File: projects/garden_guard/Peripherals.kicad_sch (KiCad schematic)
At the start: 13 parts, among them J10 Conn_02x06_Odd_Even, J11 Conn_02x01, J12 Conn_02x01, J9 Conn_02x05_Odd_Even, U11 DMN2028USS-13, U12 DMN2028USS-13

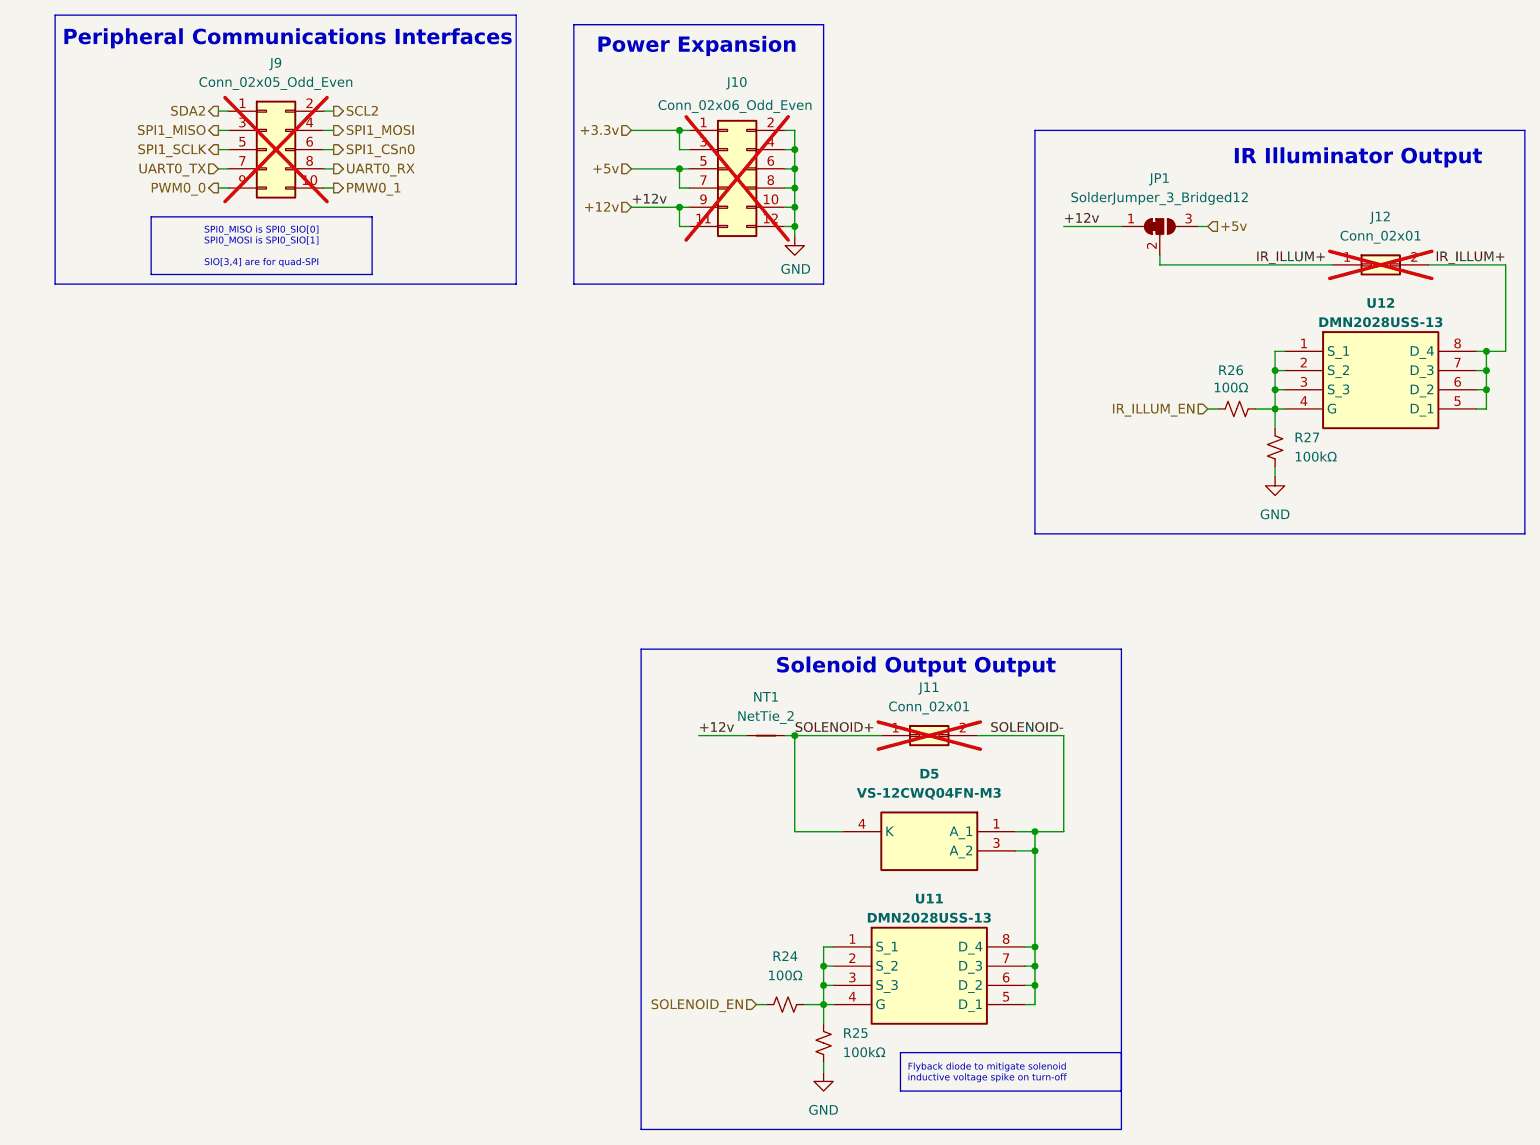
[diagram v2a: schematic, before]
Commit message: - Assign 3D models to lingering footprints lacking them - Start playing with board layout - Move CM5 library files from project to components dir
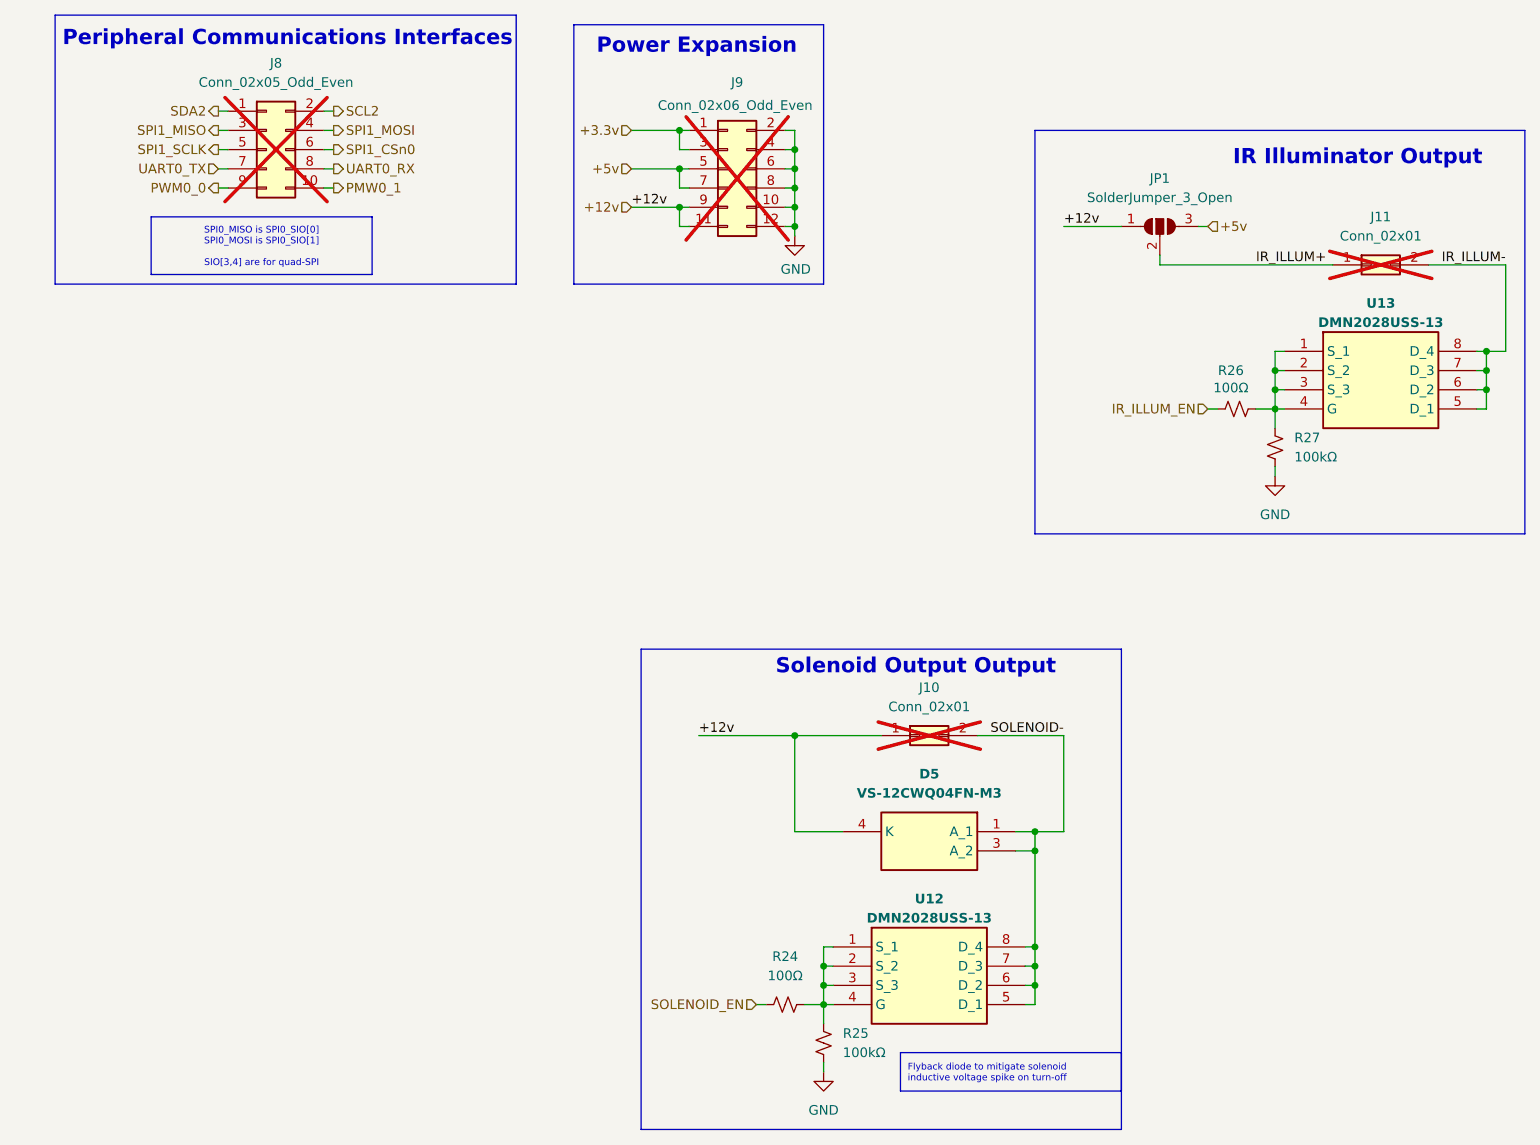
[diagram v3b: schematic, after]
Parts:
- removed JP1: SolderJumper_3_Bridged12, Jumper:SolderJumper-3_P1.3mm_Bridged12_RoundedPad1.0x1.5mm, symbol Jumper:SolderJumper_3_Bridged12
- removed NT1: NetTie_2, NetTie:NetTie-2_SMD_Pad0.5mm, symbol Device:NetTie_2
- added JP1: SolderJumper_3_Open, Jumper:SolderJumper-3_P1.3mm_Open_RoundedPad1.0x1.5mm, symbol Jumper:SolderJumper_3_Open
- renumbered J11 to J10, J12 to J11, J9 to J8, J10 to J9, U11 to U12, U12 to U13
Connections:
- net SOLENOID+ is gone; now on net +12v: D5.4 (K), J10.1 (Pin_1)
- net +12v: now also JP1.1 (A)
- net +5v: now also JP1.3 (B)
- net IR_ILLUM+: now also JP1.2 (C); no longer J11.2 (Pin_2), U13.5 (D_1), U13.6 (D_2), U13.7 (D_3), U13.8 (D_4)
- new net IR_ILLUM-: J11.2 (Pin_2), U13.5 (D_1), U13.6 (D_2), U13.7 (D_3), U13.8 (D_4)
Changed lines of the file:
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@@
 	(wire
 		(pts
-			(xy 114.3 123.19) (xy 120.65 123.19)
+			(xy 114.3 123.19) (xy 127 123.19)
 		)
 		(stroke
@@
 		(pts
 			(xy 217.17 77.47) (xy 218.44 77.47)
-		)
-		(stroke
-			(width 0)
-			(type default)
-		)
-	)
-	(wire
-		(pts
-			(xy 125.73 123.19) (xy 127 123.19)
 		)
 		(stroke
@@
 		)
 	)
-	(label "IR_ILLUM+"
+	(label "IR_ILLUM-"
 		(at 220.98 60.96 180)
 		(effects
@@
 			)
 			(justify right bottom)
-		)
-	)
-	(label "SOLENOID+"
-		(at 127 123.19 0)
-		(effects
-			(font
-				(size 1.27 1.27)
-			)
-			(justify left bottom)
 		)
 	)
@@
 	)
 	(symbol
-		(lib_id "Device:NetTie_2")
-		(at 123.19 123.19 0)
+		(lib_id "Jumper:SolderJumper_3_Open")
+		(at 175.26 55.88 0)
 		(unit 1)
 		(exclude_from_sim no)
@@
 		(dnp no)
 		(fields_autoplaced yes)
-		(property "Reference" "NT1"
-			(at 123.19 118.11 0)
-			(effects
-				(font
-					(size 1.27 1.27)
-				)
-			)
-		)
-		(property "Value" "NetTie_2"
-			(at 123.19 120.65 0)
-			(effects
-				(font
-					(size 1.27 1.27)
-				)
-			)
-		)
-		(property "Footprint" "NetTie:NetTie-2_SMD_Pad0.5mm"
-			(at 123.19 123.19 0)
+		(property "Reference" "JP1"
+			(at 175.26 49.53 0)
+			(effects
+				(font
+					(size 1.27 1.27)
+				)
+			)
+		)
+		(property "Value" "SolderJumper_3_Open"
+			(at 175.26 52.07 0)
+			(effects
+				(font
+					(size 1.27 1.27)
+				)
+			)
+		)
+		(property "Footprint" "Jumper:SolderJumper-3_P1.3mm_Open_RoundedPad1.0x1.5mm"
+			(at 175.26 55.88 0)
 			(effects
 				(font
@@
 		)
 		(property "Datasheet" "~"
-			(at 123.19 123.19 0)
-			(effects
-				(font
-					(size 1.27 1.27)
-				)
-				(hide yes)
-			)
-		)
-		(property "Description" "Net tie, 2 pins"
-			(at 123.19 123.19 0)
-			(effects
-				(font
-					(size 1.27 1.27)
-				)
-				(hide yes)
-			)
+			(at 175.26 55.88 0)
+			(effects
+				(font
+					(size 1.27 1.27)
+				)
+				(hide yes)
+			)
+		)
+		(property "Description" "Solder Jumper, 3-pole, open"
+			(at 175.26 55.88 0)
+			(effects
+				(font
+					(size 1.27 1.27)
+				)
+				(hide yes)
+			)
+		)
+		(pin "3"
+		)
+		(pin "1"
 		)
 		(pin "2"
-		)
-		(pin "1"
 		)
 		(instances
 			(project ""
 				(path "/dcdac9d4-ef08-426f-b97c-7b9219501e71/a6939206-369a-404c-88f4-a3b15aa53ce8"
-					(reference "NT1")
+					(reference "JP1")
 					(unit 1)
 				)
@@
 		(on_board yes)
 		(dnp yes)
-		(property "Reference" "J12"
+		(property "Reference" "J11"
 			(at 204.47 54.61 0)
 			(effects
@@
 			(project "garden_guard"
 				(path "/dcdac9d4-ef08-426f-b97c-7b9219501e71/a6939206-369a-404c-88f4-a3b15aa53ce8"
-					(reference "J12")
-					(unit 1)
-				)
-			)
-		)
-	)
-	(symbol
-		(lib_id "Jumper:SolderJumper_3_Bridged12")
-		(at 175.26 55.88 0)
-		(unit 1)
-		(exclude_from_sim no)
-		(in_bom no)
-		(on_board yes)
-		(dnp no)
-		(fields_autoplaced yes)
-		(property "Reference" "JP1"
-			(at 175.26 49.53 0)
-			(effects
-				(font
-					(size 1.27 1.27)
-				)
-			)
-		)
-		(property "Value" "SolderJumper_3_Bridged12"
-			(at 175.26 52.07 0)
-			(effects
-				(font
-					(size 1.27 1.27)
-				)
-			)
-		)
-		(property "Footprint" "Jumper:SolderJumper-3_P1.3mm_Bridged12_RoundedPad1.0x1.5mm"
-			(at 175.26 55.88 0)
-			(effects
-				(font
-					(size 1.27 1.27)
-				)
-				(hide yes)
-			)
-		)
-		(property "Datasheet" "~"
-			(at 175.26 55.88 0)
-			(effects
-				(font
-					(size 1.27 1.27)
-				)
-				(hide yes)
-			)
-		)
-		(property "Description" "3-pole Solder Jumper, pins 1+2 closed/bridged"
-			(at 175.26 55.88 0)
-			(effects
-				(font
-					(size 1.27 1.27)
-				)
-				(hide yes)
-			)
-		)
-		(pin "1"
-		)
-		(pin "2"
-		)
-		(pin "3"
-		)
-		(instances
-			(project ""
-				(path "/dcdac9d4-ef08-426f-b97c-7b9219501e71/a6939206-369a-404c-88f4-a3b15aa53ce8"
-					(reference "JP1")
+					(reference "J11")
 					(unit 1)
 				)
@@
 		(on_board yes)
 		(dnp yes)
-		(property "Reference" "J10"
+		(property "Reference" "J9"
 			(at 119.38 36.83 0)
 			(effects
@@
 			(project "garden_guard"
 				(path "/dcdac9d4-ef08-426f-b97c-7b9219501e71/a6939206-369a-404c-88f4-a3b15aa53ce8"
-					(reference "J10")
+					(reference "J9")
 					(unit 1)
 				)
@@
 		(on_board yes)
 		(dnp no)
-		(property "Reference" "U12"
+		(property "Reference" "U13"
 			(at 204.47 66.04 0)
 			(effects
@@
 			(project "garden_guard"
 				(path "/dcdac9d4-ef08-426f-b97c-7b9219501e71/a6939206-369a-404c-88f4-a3b15aa53ce8"
-					(reference "U12")
+					(reference "U13")
 					(unit 1)
 				)
@@
 		(dnp yes)
 		(fields_autoplaced yes)
-		(property "Reference" "J9"
+		(property "Reference" "J8"
 			(at 58.42 34.29 0)
 			(effects
@@
 			(project "garden_guard"
 				(path "/dcdac9d4-ef08-426f-b97c-7b9219501e71/a6939206-369a-404c-88f4-a3b15aa53ce8"
-					(reference "J9")
+					(reference "J8")
 					(unit 1)
 				)
@@
 		(on_board yes)
 		(dnp yes)
-		(property "Reference" "J11"
+		(property "Reference" "J10"
 			(at 144.78 116.84 0)
 			(effects
@@
 			(project "garden_guard"
 				(path "/dcdac9d4-ef08-426f-b97c-7b9219501e71/a6939206-369a-404c-88f4-a3b15aa53ce8"
-					(reference "J11")
+					(reference "J10")
 					(unit 1)
 				)
@@
 		(on_board yes)
 		(dnp no)
-		(property "Reference" "U11"
+		(property "Reference" "U12"
 			(at 144.78 144.78 0)
 			(effects
@@
 			(project "garden_guard"
 				(path "/dcdac9d4-ef08-426f-b97c-7b9219501e71/a6939206-369a-404c-88f4-a3b15aa53ce8"
-					(reference "U11")
+					(reference "U12")
 					(unit 1)
 				)

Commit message: - Add M.2 power and connector layout - Add micro HDMI to schematic and layout - Add microSD layout - Add IR illuminator and solenoid output MOSFET layouts - Add USB-C layout
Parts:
- removed D5: VS-12CWQ04FN-M3, Custom_Switch:VS-12CWQ04FN-M3, symbol Custom_Switch:VS-12CWQ04FN-M3
- added D6: SS34, Diode_SMD:D_SMA, symbol Diode:SS34
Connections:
- net +12v: now also D6.1 (K)
- net GND: now also U12.1 (S_1), U12.2 (S_2), U12.3 (S_3), U13.1 (S_1), U13.2 (S_2), U13.3 (S_3)
- net SOLENOID-: now also D6.2 (A)
- net at R26.1, R27.1, U13.4 (G): no longer U13.1 (S_1), U13.2 (S_2), U13.3 (S_3)
- net at R24.2, R25.1, U12.4 (G): no longer U12.1 (S_1), U12.2 (S_2), U12.3 (S_3)
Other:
- note added: "Solenoid Output"
- note removed: "Solenoid Output Output"
